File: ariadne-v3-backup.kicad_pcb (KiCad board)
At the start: 2 copper layers, 186.8 x 207 mm, 98 parts, among them J1 Conn_01x05_Male, J2 Conn_01x05_Male, J3 Conn_01x05_Male, J4 Conn_01x05_Male, J5 Conn_01x05_Male, Q1 IRF5305-Reverse-Polarity, U1 Noctua-NF-A4x10-Simple-Fan-ar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, U10 OKI-78SR-12v, U11 OKI-78SR-5v, U12 Meanwell-LDD-1200LW-connector, U13 12v-Connector, U14 Meanwell-LDD-1200LW-connector, U15 12v-Connector, U16 Connector-LED, U17 Connector-LED, U18 Meanwell-LDD-1200LW, U19 Meanwell-LDD-1200LW, U2 Meanwell-LDD-1200LW-connector, U20 Meanwell-LDD-1200LW-connector, U21 Meanwell-LDD-1200LW-connector, U22 Meanwell-LDD-1200LW-connector, U23 Meanwell-LDD-1200LW-connector, U24 ESP32-WROOM-32D, U25 Connector-LED, U26 Connector-LED, U27 Meanwell-LDD-1200LW, U28 Meanwell-LDD-1200LW, U29 Noctua-NF-A4x10-Fan-mech-aria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, U3 POWER_CONNECTOR-DCJ250-20-B-K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, U33 Noctua-NF-A4x10-Simple-Fan-ar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, U34 Noctua-NF-A4x10-Simple-Fan-ar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, U35 Bridgelux-Vero-18-mech-v3-ari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, U4 Noctua-NF-A4x10-Simple-Fan-ar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, U43 Noctua-NF-A4x10-Simple-Fan-ar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, U44 Noctua-NF-A4x10-Simple-Fan-ar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, U45 12v-Connector_copy, U47 12v-Connector_copy, U5 Meanwell-LDD-1200LW-connector, U6 Connector-LED, U7 Connector-LED, U8 Meanwell-LDD-1200LW, U9 Meanwell-LDD-1200LW

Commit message: now for real
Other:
- board size 186.8 x 207 mm -> 186.4 x 206.6 mm
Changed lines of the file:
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@@
   (general
     (thickness 1.6)
-    (drawings 124)
+    (drawings 119)
     (tracks 1479)
     (zones 0)
@@
   (gr_line (start 176.5 156.9) (end 176.5 196.9) (layer Edge.Cuts) (width 0.1))
   (gr_line (start 93.7 156.9) (end 176.5 156.9) (layer Edge.Cuts) (width 0.1))
-  (gr_line (start 176.71 -9.72) (end 176.9 -9.72) (layer Margin) (width 0.15))
-  (gr_line (start 176.9 197.3) (end 176.9 -9.72) (layer Edge.Cuts) (width 0.15))
-  (gr_line (start -9.93 197.3) (end 176.9 197.3) (layer Edge.Cuts) (width 0.15))
-  (gr_line (start -9.93 -9.72) (end -9.93 197.3) (layer Edge.Cuts) (width 0.15))
-  (gr_line (start -9.93 -9.72) (end 176.71 -9.72) (layer Edge.Cuts) (width 0.15))
   (gr_line (start 117.1 133.445) (end 117.1 97.245) (layer F.SilkS) (width 0.15))
   (gr_line (start 153.5 97.245) (end 153.5 132.645) (layer F.SilkS) (width 0.15))

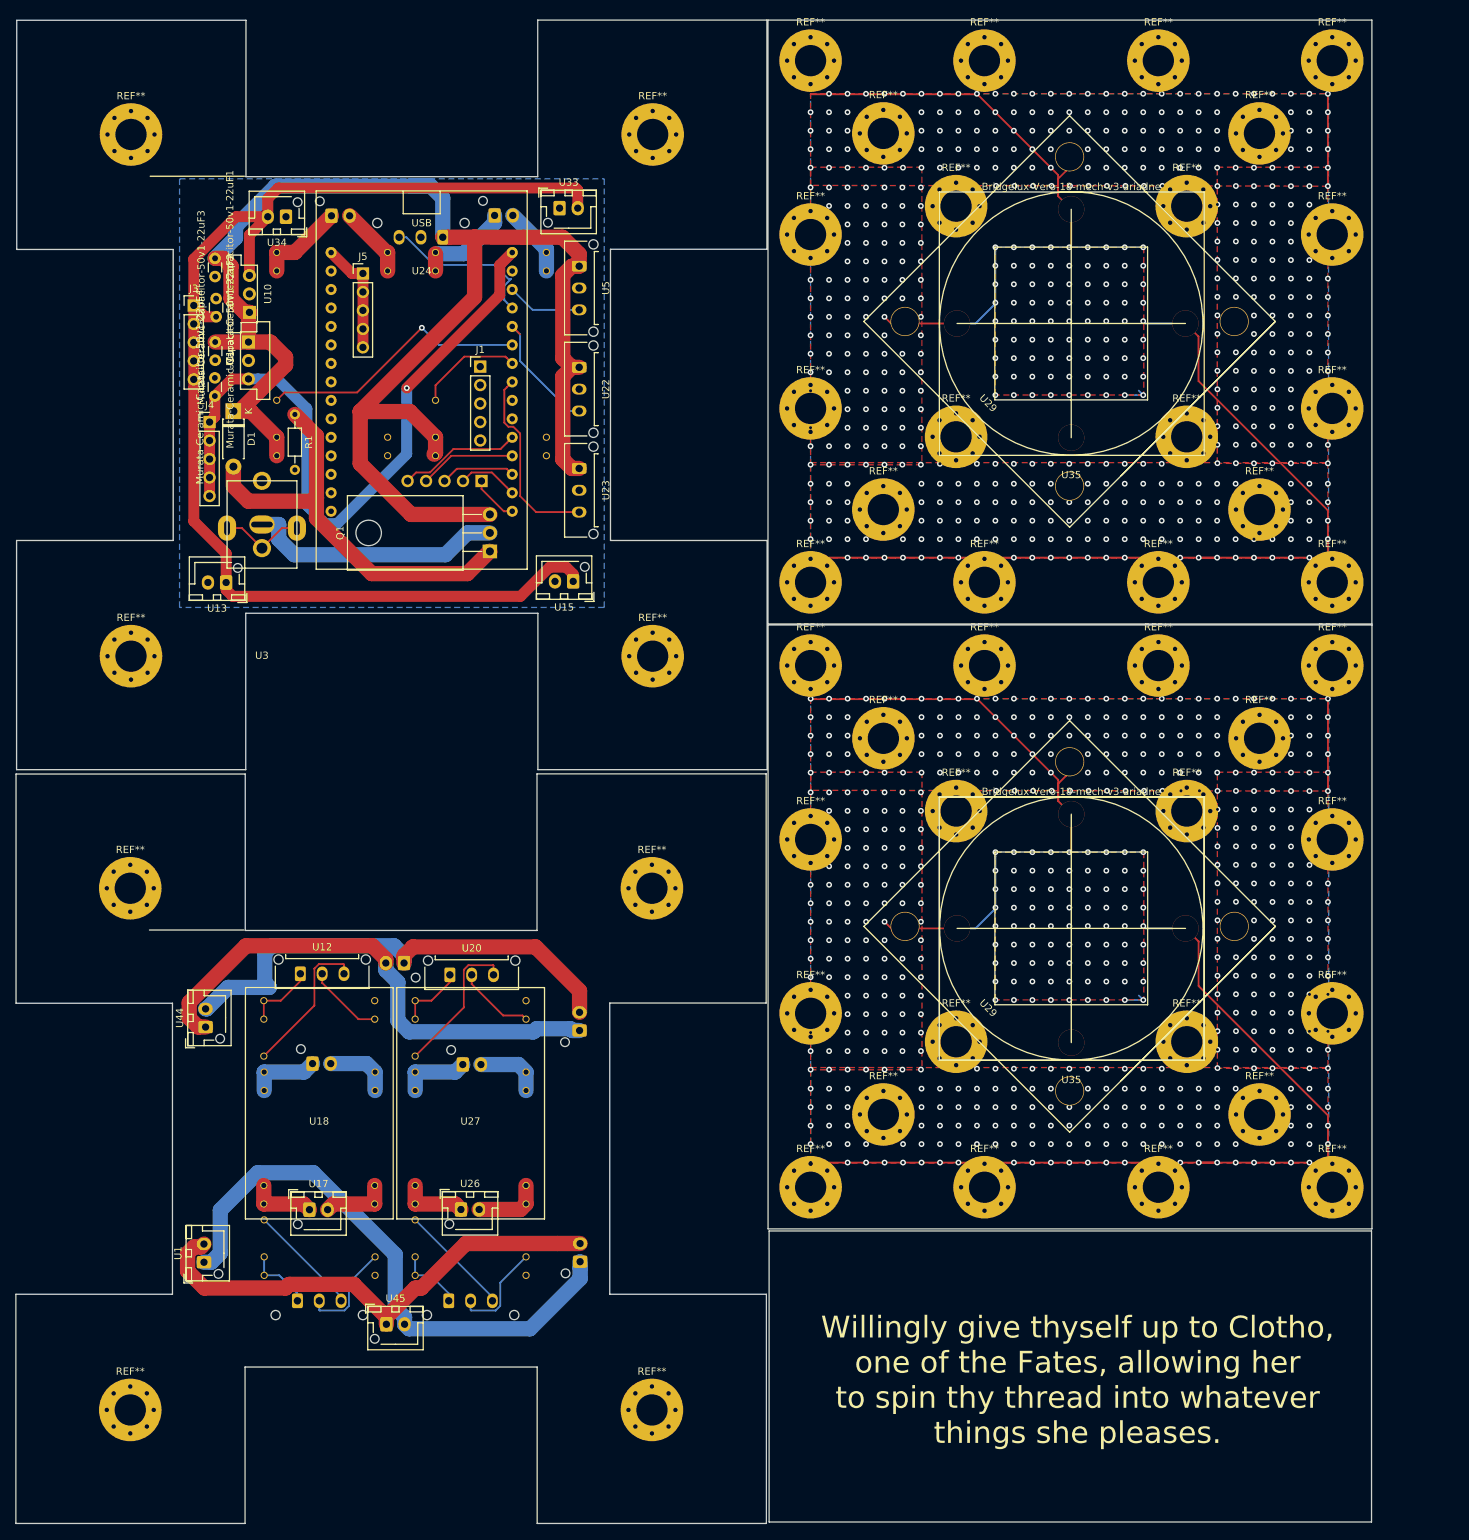
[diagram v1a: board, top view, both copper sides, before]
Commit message: Fourth version, footprint of LED driver was flipped. Gave some cleareance to the ground plane, re arranged some paths.
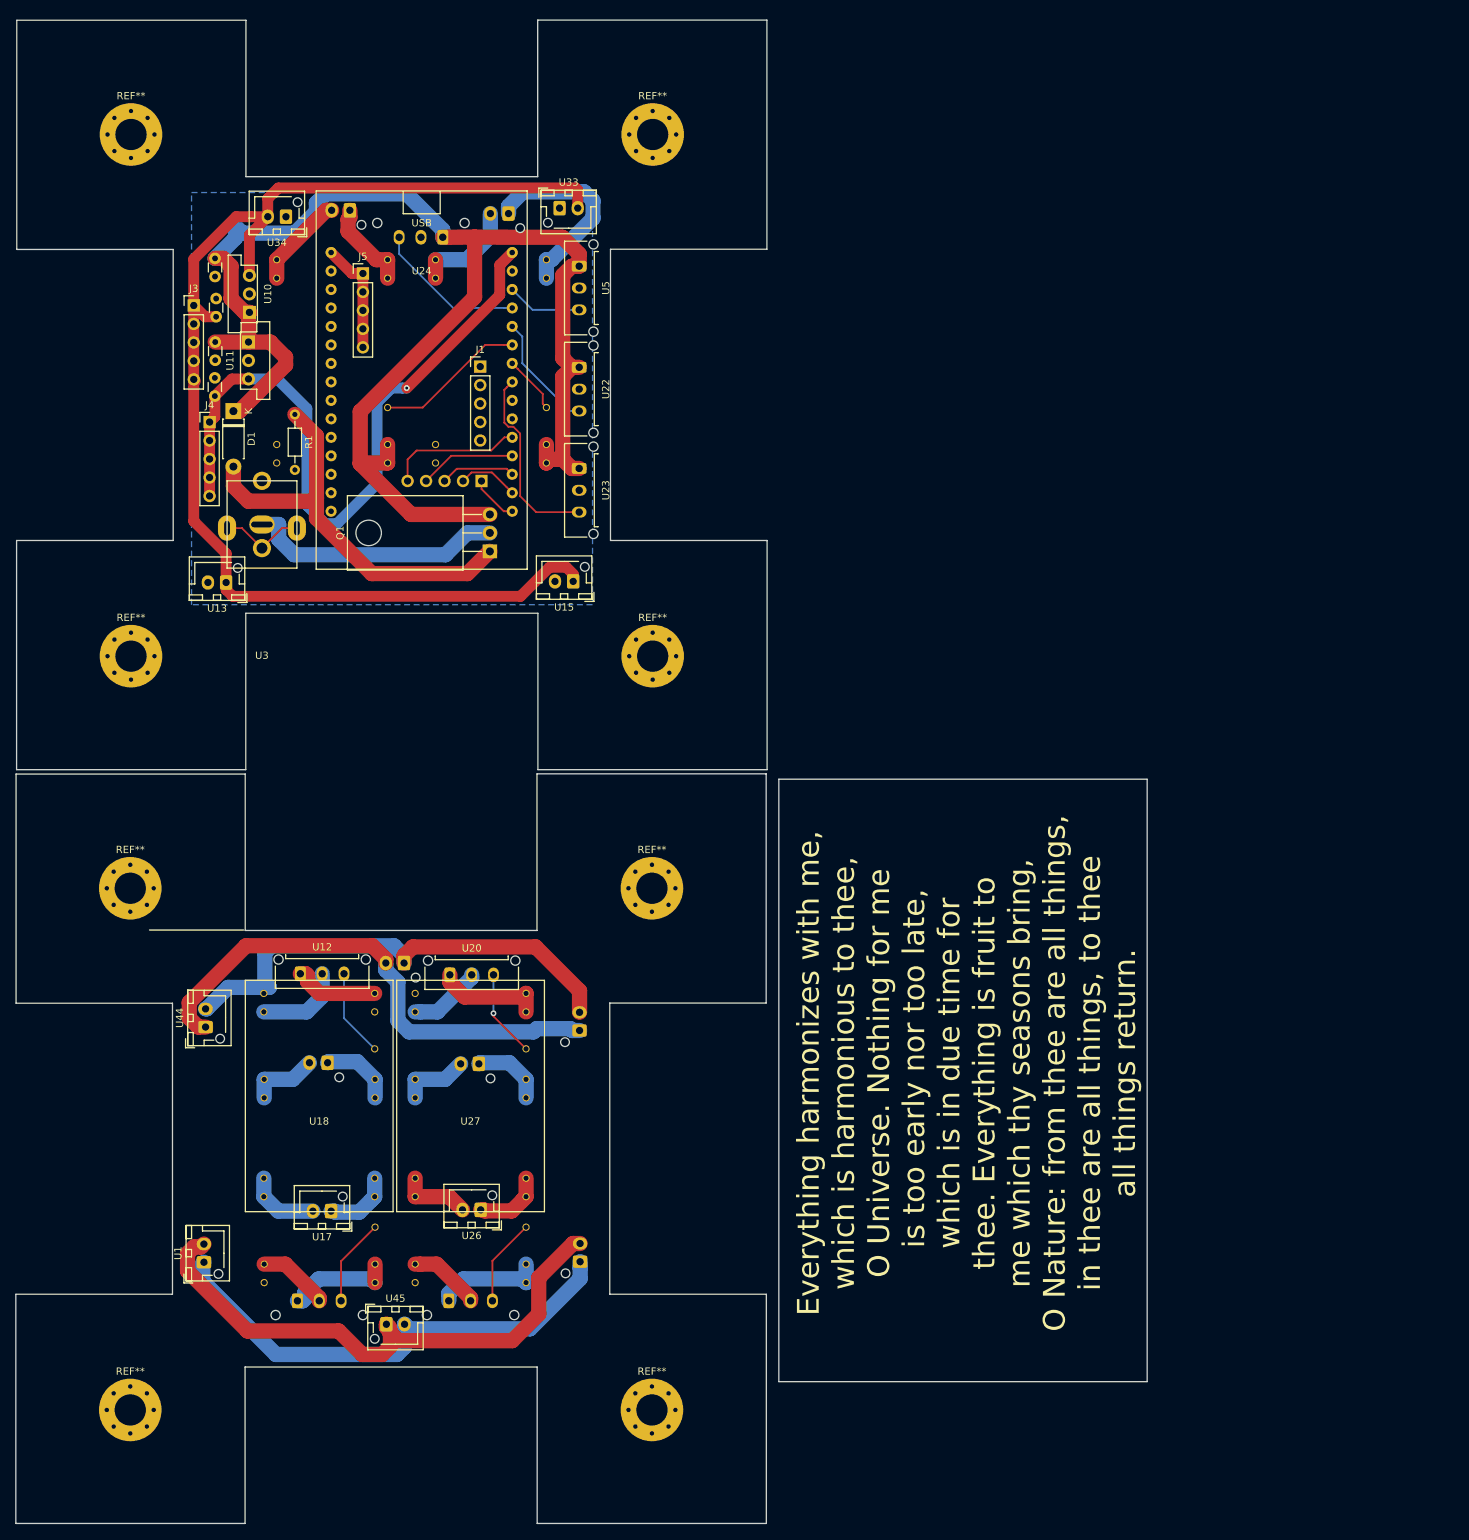
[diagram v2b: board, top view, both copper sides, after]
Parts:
- removed the REF** at (109.4, 140.9)
- removed the REF** at (147.2, 79.2)
- removed the REF** at (99.4, 103.1)
- removed the REF** at (123.3, 150.9)
- removed the REF** at (123.3, 79.2)
- removed the REF** at (99.4, 79.2)
- removed the REF** at (171.1, 103.1)
- removed the REF** at (151.1, 130.9)
- removed the REF** at (151.1, 99.2)
- removed the REF** at (119.4, 130.9)
- removed the REF** at (119.4, 99.2)
- removed the REF** at (109.4, 89.2)
- removed the REF** at (161.1, 140.9)
- removed the REF** at (119.4, 47.8)
- removed the REF** at (151.1, 16.1)
- removed the REF** at (171.1, 19.9)
- removed the REF** at (151.1, 47.8)
- removed the REF** at (119.4, 16.1)
- removed the REF** at (99.4, 127.0)
- removed the REF** at (161.1, 57.8)
- removed the REF** at (109.4, 57.8)
- removed the REF** at (161.1, 6.05)
- removed the REF** at (109.4, 6.05)
- removed the REF** at (171.1, 67.8)
- removed the REF** at (147.2, 67.8)
- removed the REF** at (123.3, 67.8)
- removed the REF** at (99.4, 67.8)
- removed the REF** at (171.1, 43.9)
- removed the REF** at (99.4, 43.9)
- removed the REF** at (171.1, 79.2)
- removed the REF** at (99.4, 19.9)
- removed the REF** at (171.1, -3.95)
- removed the REF** at (147.2, -3.95)
- removed the REF** at (123.3, -3.95)
- removed the REF** at (99.4, -3.95)
- removed the REF** at (171.1, 150.9)
- removed the REF** at (147.2, 150.9)
- removed the REF** at (161.1, 89.2)
- removed the REF** at (99.4, 150.9)
- removed the REF** at (171.1, 127.0)
- removed U29 (x2): Noctua-NF-A4x10-Fan-mech-ariadne, ariadne:Noctua-NF-A4x10-mech
- removed U35 (x2): Bridgelux-Vero-18-mech-v3-ariadne, ariadne:Vero-18-mech
- moved U17 2.98 mm to (33.5, 154.2), turned to 180 degrees
- moved U26 2.71 mm to (54.1, 154.0), turned to 180 degrees
- moved U7 2.64 mm to (36.1, 16.6), turned to 180 degrees
- moved U6 2.21 mm to (53.8, 133.9), turned to 180 degrees
- moved U25 2.07 mm to (33.0, 133.8), turned to 180 degrees
- moved U16 1.93 mm to (57.9, 17.1), turned to 180 degrees
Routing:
- net Net-(U35-Pad0): track 204.2 -> 0.00 mm, vias 435 -> 0
- net (no net): track 204.2 -> 0.00 mm, vias 665 -> 0
- net VIN+Master1: track 220.5 -> 200.4 mm
- net DIM-4: track 37.5 -> 20.7 mm, vias 1 -> 0
- net LDD_5-OUT+: track 13.0 -> 27.7 mm
- net FAN2-: track 79.2 -> 67.7 mm
- net FAN2+: track 67.4 -> 77.9 mm
- net Net-(U12-Pad3): track 20.5 -> 12.1 mm
- net Net-(U20-Pad3): track 20.3 -> 12.0 mm, vias 0 -> 1
- net DIM-5: track 14.6 -> 8.01 mm
- net Net-(U2-Pad1): track 9.20 -> 15.2 mm
- net Net-(U21-Pad1): track 9.15 -> 15.2 mm
- net Net-(U20-Pad1): track 9.37 -> 15.1 mm
- net LDD_5-OUT-: track 9.54 -> 14.5 mm
- net Net-(U21-Pad2): track 13.9 -> 9.88 mm
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- removed copper zone on B.Cu, net (none)
- removed copper zone on F.Cu, net (none)
- removed copper zone on B.Cu, net Net-(U35-Pad0)
- removed copper zone on F.Cu, net Net-(U35-Pad0)
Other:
- board size 186.4 x 206.6 mm -> 155.5 x 206.6 mm
- net class Default: clearance 0.2 -> 0.5
- rule trace_clearance: 0.2 -> 0.5
- board text added: ""Unhappy am I because this has happened to me". Not so, but happy am I, though this has happened to me, because I continue free from pain, neither crushed by the present nor fearing the future."
- board text added: "Everything harmonizes with me, which is harmonious to thee, O Universe. Nothing for me is too early nor too late, which is in due time for thee. Everything is fruit to me which thy seasons bring, O Nature: from thee are all things, in thee are all things, to thee all things return."
- board text removed: "Be like the promontory against which the waves continually break, but it stands firm and tames the fury of the water around it."
- board text removed: "Willingly give thyself up to Clotho, one of the Fates, allowing her to spin thy thread into whatever things she pleases."
